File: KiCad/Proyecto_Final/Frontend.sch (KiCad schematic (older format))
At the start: 70 parts, among them J1 RF_IN, Q1 BSS315P, T1 B0310J50100AHF, T2 B0310J50100AHF, U1 SKY13351, U2 RFFC5072, U3 SKY13351, U4 SKY13351, U5 SKY13351, U6 SKY13351, U7 SKY13351, U8 MAAL-010200

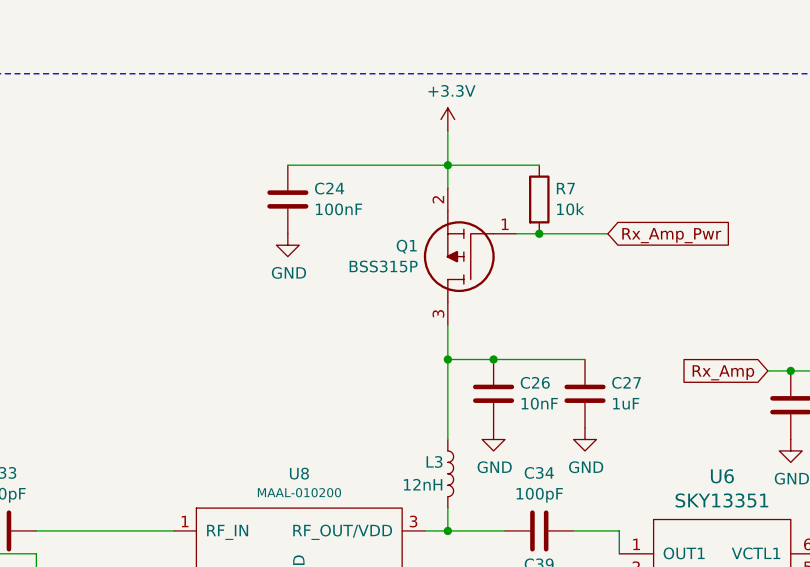
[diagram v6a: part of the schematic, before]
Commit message: Reasignación de footprints por cambio de proveedor de componentes (JLCPCB SMT Assembly).
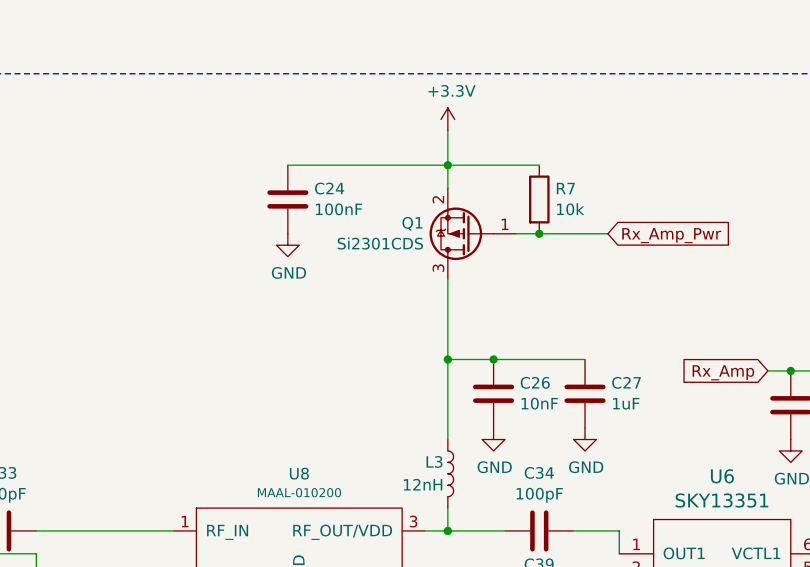
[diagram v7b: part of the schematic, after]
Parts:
- removed Q1: BSS315P, SamacSys_Parts:SOT95P237X112-3N, symbol SamacSys_Parts:BSS315PH6327XTSA1
- added Q1: Si2301CDS, Package_TO_SOT_SMD:SOT-23, symbol Transistor_FET:Si2319CDS
- C18: footprint Capacitor_SMD:C_0402_1005Metric -> Capacitor_SMD:C_0603_1608Metric
- C27: footprint Capacitor_SMD:C_0805_2012Metric -> Capacitor_SMD:C_0402_1005Metric
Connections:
- net +3V3: now also Q1.2 (S)
- net Rx_Amp_Pwr: now also Q1.1 (G)
- net at C26.1, C27.1, L3.1: now also Q1.3 (D)
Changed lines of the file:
@@
 F 0 "C18" H 1665 4346 50  0000 L CNN
 F 1 "8.2pF" H 1665 4255 50  0000 L CNN
-F 2 "Capacitor_SMD:C_0402_1005Metric" H 1588 4150 50  0001 C CNN
+F 2 "Capacitor_SMD:C_0603_1608Metric" H 1588 4150 50  0001 C CNN
 F 3 "~" H 1550 4300 50  0001 C CNN
 	1    1550 4300
@@
 F 0 "C27" H 8615 7596 50  0000 L CNN
 F 1 "1uF" H 8615 7505 50  0000 L CNN
-F 2 "Capacitor_SMD:C_0805_2012Metric" H 8538 7400 50  0001 C CNN
+F 2 "Capacitor_SMD:C_0402_1005Metric" H 8538 7400 50  0001 C CNN
 F 3 "~" H 8500 7550 50  0001 C CNN
 	1    8500 7550
@@
 Wire Wire Line
 	7800 8150 7900 8150
-$Comp
-L SamacSys_Parts:BSS315PH6327XTSA1 Q1
-U 1 1 60253009
-P 8200 6850
-F 0 "Q1" H 8630 6904 50  0000 L CNN
-F 1 "BSS315P" H 8630 6995 50  0000 L CNN
-F 2 "SamacSys_Parts:SOT95P237X112-3N" H 8650 6800 50  0001 L CNN
-F 3 "" H 8650 6700 50  0001 L CNN
-F 4 "INFINEON - BSS315PH6327XTSA1 - Power MOSFET, P Channel, 30 V, 1.5 A, 0.113 ohm, SOT-23, Surface Mount" H 8650 6600 50  0001 L CNN "Description"
-F 5 "1.12" H 8650 6500 50  0001 L CNN "Height"
-F 6 "726-BSS315PH6327" H 8650 6400 50  0001 L CNN "Mouser Part Number"
-F 7 "https://www.mouser.co.uk/ProductDetail/Infineon-Technologies/BSS315PH6327XTSA1?qs=K00xGehIljvgHRyAng%252B8Qw%3D%3D" H 8650 6300 50  0001 L CNN "Mouser Price/Stock"
-F 8 "Infineon" H 8650 6200 50  0001 L CNN "Manufacturer_Name"
-F 9 "BSS315PH6327XTSA1" H 8650 6100 50  0001 L CNN "Manufacturer_Part_Number"
-	1    8200 6850
-	-1   0    0    1
-$EndComp
 Wire Wire Line
 	7900 8050 7900 8150
@@
 Wire Wire Line
 	7900 7400 7900 7750
-Wire Wire Line
-	7900 7250 7900 7400
 Connection ~ 7900 7400
 Wire Wire Line
@@
 Wire Notes Line
 	650  10700 4100 10700
+$Comp
+L Transistor_FET:Si2319CDS Q1
+U 1 1 60AADA1B
+P 8000 6850
+F 0 "Q1" H 8205 6804 50  0000 L CNN
+F 1 "Si2301CDS" H 8205 6895 50  0000 L CNN
+F 2 "Package_TO_SOT_SMD:SOT-23" H 8200 6775 50  0001 L CIN
+F 3 "http://www.vishay.com/docs/66709/si2319cd.pdf" H 8000 6850 50  0001 L CNN
+	1    8000 6850
+	-1   0    0    1
+$EndComp
+Wire Wire Line
+	7900 7050 7900 7400
 $EndSCHEMATC

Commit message: Sección RF terminada.
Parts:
- removed R2: 10k, Resistor_SMD:R_0402_1005Metric, symbol Device:R
- renumbered C17 to C13, C13 to C14, C14 to C15, C15 to C16, C16 to C17, R3 to R2, R4 to R3, R5 to R4, R6 to R5, R7 to R6
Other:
- moved on the sheet: C13
